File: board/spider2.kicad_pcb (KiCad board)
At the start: 2 copper layers, 137 x 75.5 mm, 121 parts, among them J1 NRJ6HH-1, J10 PJ-320A, J11 PJ358, J12 PJ358, J13 PJ358, J14 PJ358, J15 PJ358, J16 PJ358, J19 PJ358, J2 NRJ6HH-1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

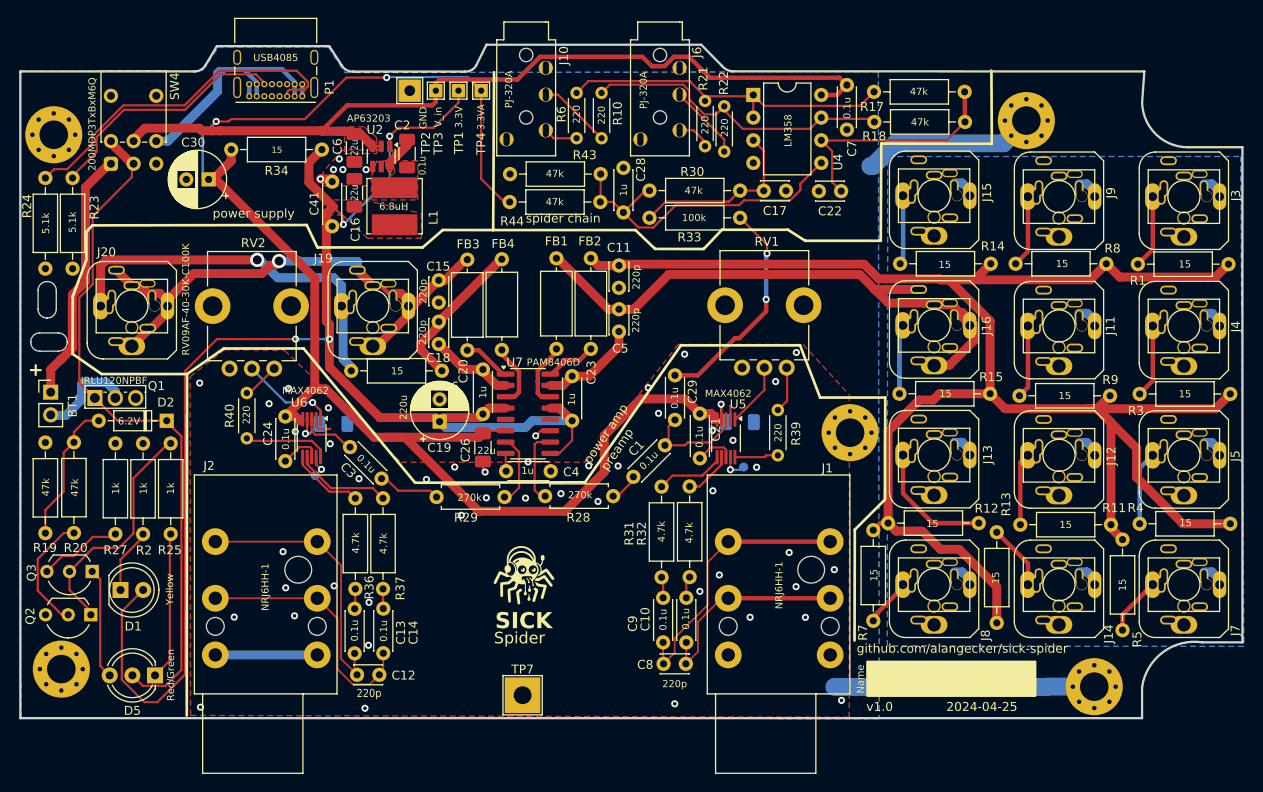
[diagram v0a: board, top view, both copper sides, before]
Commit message: shorter traces + silkscreen updates
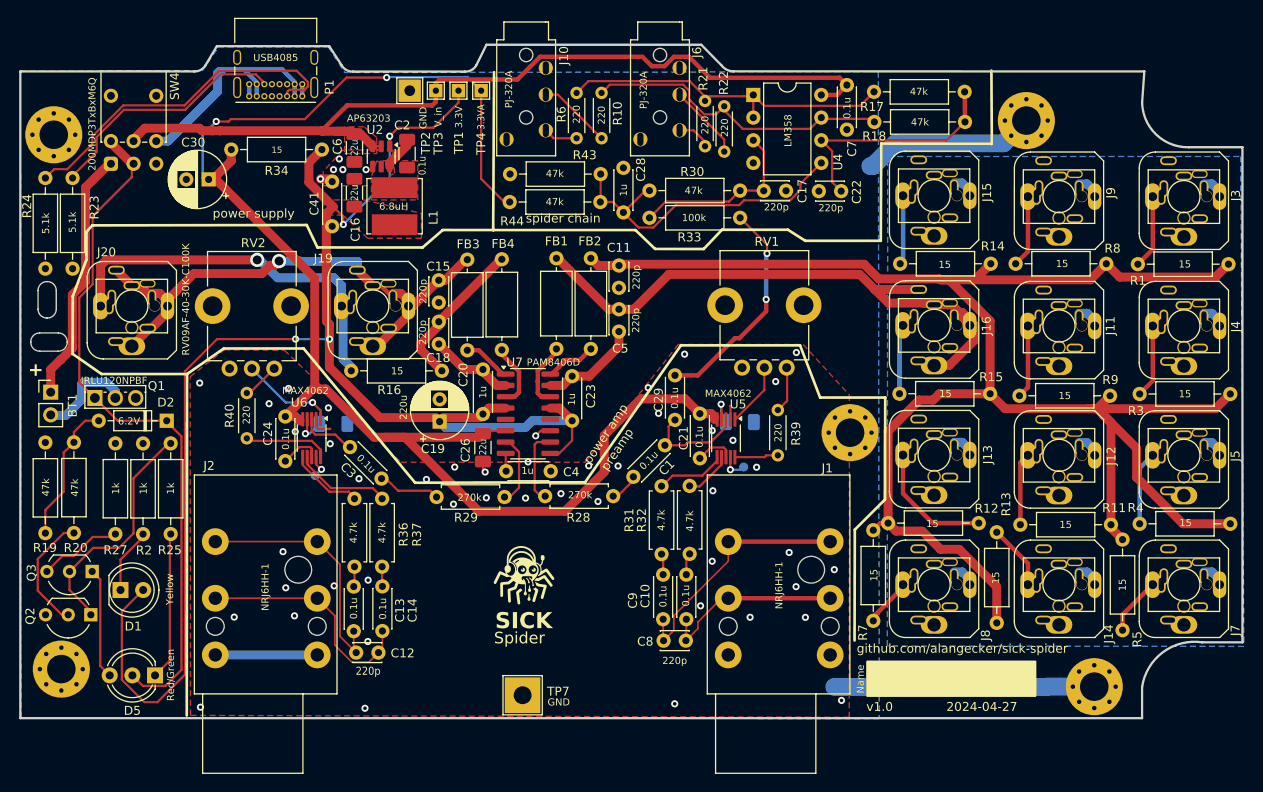
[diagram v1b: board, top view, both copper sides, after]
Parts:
- R31, R32, R36, R37: footprint Resistor_THT:R_Axial_DIN0207_L6.3mm_D2.5mm_P10.16mm_Horizontal -> Resistor_THT:R_Axial_DIN0207_L6.3mm_D2.5mm_P7.62mm_Horizontal
- moved R32 2.60 mm to (212.7, 84.7)
- moved C10 2.60 mm to (212.3, 92.0)
- moved C8 2.60 mm to (209.8, 94.4)
- moved C9 2.60 mm to (209.7, 92.0)
- moved R31 2.60 mm to (209.5, 84.7)
- moved C14 2.49 mm to (178.2, 93.3)
- moved C12 2.49 mm to (175.3, 95.7)
- moved R37 2.49 mm to (178.2, 86.1)
- moved C13 2.49 mm to (175.0, 93.3)
- moved R36 2.49 mm to (175.1, 86.1)
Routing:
- net /Preamp Interpreter/IN+: track 30.6 -> 28.0 mm
- net /Preamp Interpreter/IN-: track 23.6 -> 21.0 mm
- net /Preamp Floor/IN-: track 28.8 -> 26.2 mm
- net /Preamp Floor/IN+: track 30.7 -> 28.2 mm
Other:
- board text added: "2024-04-27"
- board text removed: "2024-04-25"

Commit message: clearer separation of sections, test marks,...
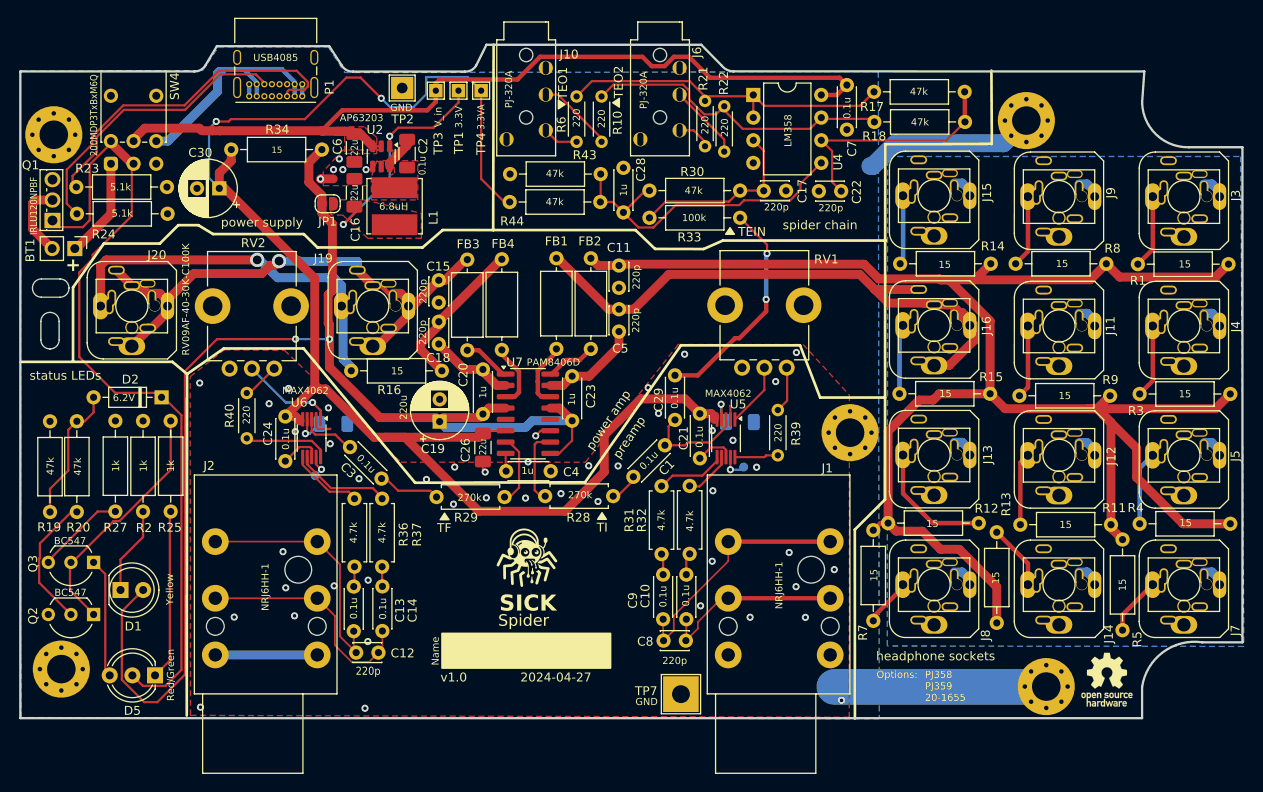
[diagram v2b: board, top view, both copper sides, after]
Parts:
- removed C41: dnp, Capacitor_THT:C_Disc_D4.3mm_W1.9mm_P5.00mm
- added JP1: ~, Jumper:SolderJumper-2_P1.3mm_Open_RoundedPad1.0x1.5mm, F.Cu at (172.1, 45.4)
- added REF**: OSHW-Logo_5.7x6mm_SilkScreen, Symbol:OSHW-Logo_5.7x6mm_SilkScreen, F.Cu at (259.4, 98.8)
- added REF**: OSHW-Logo2_7.3x6mm_SilkScreen, Symbol:OSHW-Logo2_7.3x6mm_SilkScreen, B.Cu at (205.8, 99.2)
- FB2, FB3, FB4: value 3A, >100 Ohm@100MHz -> 3A/≥100 Ohm
- moved Q1 20.5 mm to (141.2, 47.3), turned to 90 degrees
- moved TP7 17.8 mm to (211.7, 100.4)
- moved BT1 16.3 mm to (143.8, 50.5), turned to -90 degrees
- moved R24 15.0 mm to (154.2, 46.5), turned to 180 degrees
- moved R23 14.0 mm to (154.1, 43.5), turned to 180 degrees
- moved H4 5.38 mm to (252.7, 99.5)
- moved D2 2.69 mm to (153.5, 67.1)
- moved R25 2.53 mm to (154.5, 79.9)
- moved R27 2.53 mm to (148.3, 79.9)
- moved R2 2.52 mm to (151.4, 69.8)
- moved R19 2.43 mm to (141.0, 80.0)
- moved R20 2.38 mm to (144.0, 69.8)
- moved C30 1.56 mm to (159.9, 43.7)
- moved Q3 1.03 mm to (145.9, 85.6)
- moved TP2 0.90 mm to (180.4, 32.5)
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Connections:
- C16 pad 2: +3.3V -> Net-(JP1-A)
- L1 pad 2: +3.3V -> Net-(JP1-A)
- TP1 pad 1: +3.3V -> Net-(JP1-A)
- U2 pad 1: +3.3V -> Net-(JP1-A)
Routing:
- net +3.3V: track 171.8 -> 145.1 mm, vias 4 -> 2
- net Net-(JP1-A): track 0.00 -> 26.4 mm, vias 0 -> 2
- net Net-(BT1-+): track 28.3 -> 11.3 mm
- net +BATT: track 77.5 -> 91.8 mm
- net GND: track 101.3 -> 96.0 mm, vias 51 -> 50
- net +3.3VA: track 167.5 -> 170.7 mm
- net Net-(P1-CC): track 39.0 -> 41.6 mm
- net Net-(BT1--): track 11.0 -> 8.39 mm
- net Net-(D5-K1): track 16.6 -> 19.1 mm
- net Net-(D1-K): track 7.31 -> 9.84 mm
- net Net-(Q2-B): track 13.3 -> 15.1 mm
- net Net-(Q2-C): track 26.7 -> 27.9 mm
- net Net-(P1-VCONN): track 27.9 -> 29.1 mm
- net Net-(D5-K2): track 12.5 -> 13.4 mm
- net Net-(D2-A): track 16.0 -> 15.4 mm
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- added copper zone on F.Cu, net Net-(JP1-A)
- removed copper zone on F.Cu, net +3.3V
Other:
- outline, holes or cut-outs redrawn
- board text added: "Options:"
- board text added: "PJ358 PJ359 20-1655"
- board text added: "TEIN"
- board text added: "TEO1"
- board text added: "TEO2"
- board text added: "TF"
- board text added: "TI"
- board text added: "headphone sockets"
- board text added: "status LEDs"

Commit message: some cleanups, cheaper MOSFET,  datasheet links,
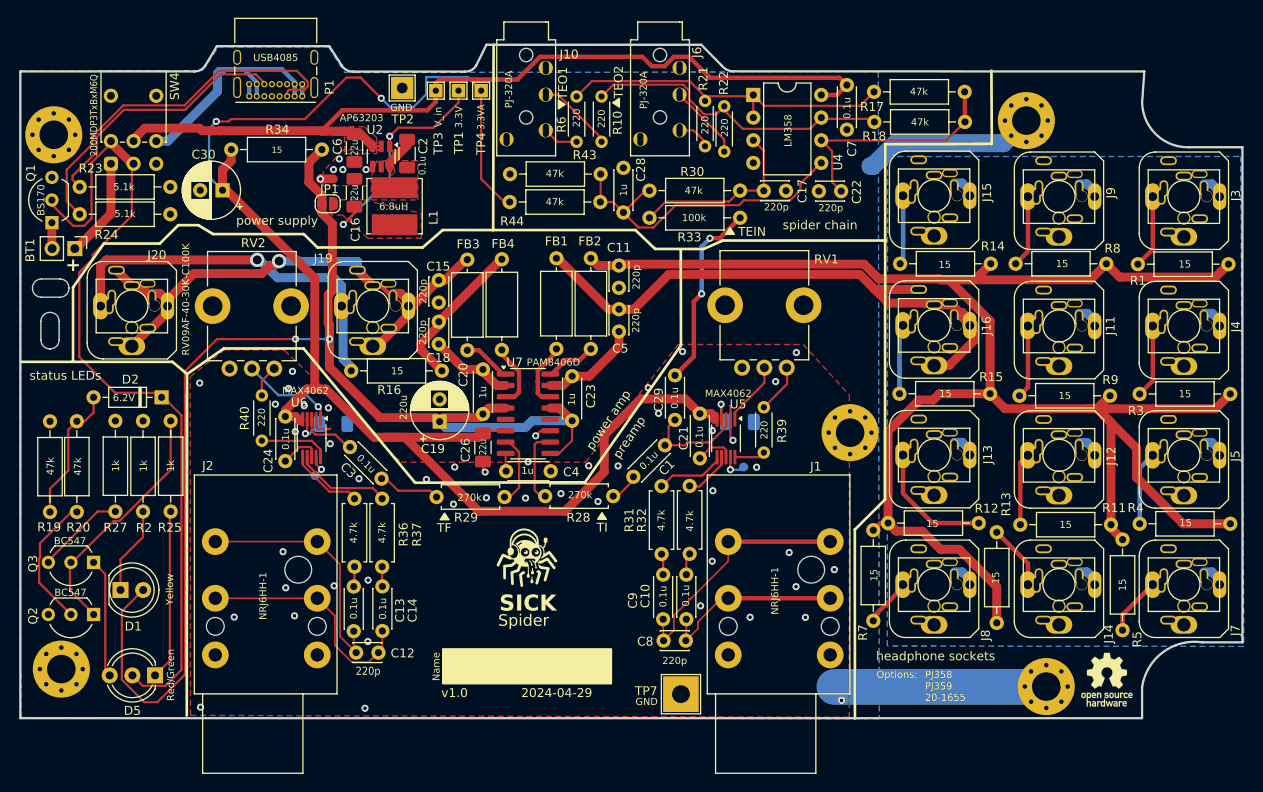
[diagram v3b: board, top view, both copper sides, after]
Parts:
- J1, J2: footprint Connector_Audio:Jack_6.35mm_Neutrik_NRJ6HH_Horizontal -> Connector_Audio:Jack_6.35mm_Neutrik_NRJ6HH-1_Horizontal
- Q1: value IRLU120NPBF -> BS170; footprint Package_TO_SOT_THT:TO-251-3_Vertical -> Package_TO_SOT_THT:TO-92_Inline_Wide
- moved R40 1.71 mm to (164.7, 72.0)
- moved R39 1.60 mm to (221.0, 73.3)
- moved C30 0.42 mm to (160.3, 43.9)
- moved R23 0.38 mm to (154.5, 43.5)
- moved R24 0.31 mm to (154.5, 46.6)
- moved Q1 0.26 mm to (141.2, 47.5)
- renumbered REF** to LOGO1, REF** to LOGO2
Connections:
- Q1 pad 1: +BATT -> Net-(BT1--)
- Q1 pad 2: Net-(BT1--) -> +BATT
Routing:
- net GND: track 96.0 -> 87.0 mm, vias 50 -> 52
- net Net-(BT1--): track 8.39 -> 2.91 mm
- net Net-(C29-Pad1): track 25.0 -> 21.3 mm
- net Net-(U6-G1): track 9.62 -> 7.82 mm
- net Net-(U5-G1): track 4.89 -> 3.45 mm
- net +BATT: track 91.8 -> 93.0 mm
- net Net-(R40-Pad2): track 4.20 -> 3.58 mm
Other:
- board text added: "2024-04-29"
- board text removed: "2024-04-27"

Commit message: 1.0: fixing wrong NRJ6HH-1 symbol
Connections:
- J1 pad G: (no net) -> GND
- J2 pad G: (no net) -> GND
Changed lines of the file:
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@@
 			)
 		)
-		(property "Datasheet" "https://www.neutrik.com/media/9131/download/st-nrj6hh-1.PDF?v=2"
+		(property "Datasheet" "https://www.neutrik.com/en/product/nrj6hh-1"
 			(at 0 0 -90)
 			(unlocked yes)
@@
 			)
 		)
-		(property "Description" "Slim Jacks, 6.35mm (1/4in) stereo jack, switched, half threaded nose"
+		(property "Description" "Slim Jacks, 6.35mm (1/4in) stereo jack, switched, half threaded nose, sleeve contact/front panel connection"
 			(at 0 0 -90)
 			(unlocked yes)
@@
 			(layers "*.Cu" "*.Mask")
 			(remove_unused_layers no)
+			(net 4 "GND")
+			(pintype "passive")
 		)
 		(pad "R" thru_hole circle
@@
 			)
 		)
-		(property "Datasheet" "https://www.neutrik.com/en/product/nrj6hh"
+		(property "Datasheet" "https://www.neutrik.com/en/product/nrj6hh-1"
 			(at 0 0 -90)
 			(unlocked yes)
@@
 			)
 		)
-		(property "Description" "Slim Jacks, 6.35mm (1/4in) stereo jack, switched, half threaded nose"
+		(property "Description" "Slim Jacks, 6.35mm (1/4in) stereo jack, switched, half threaded nose, sleeve contact/front panel connection"
 			(at 0 0 -90)
 			(unlocked yes)
@@
 			(layers "*.Cu" "*.Mask")
 			(remove_unused_layers no)
+			(net 4 "GND")
+			(pintype "passive")
 		)
 		(pad "R" thru_hole circle

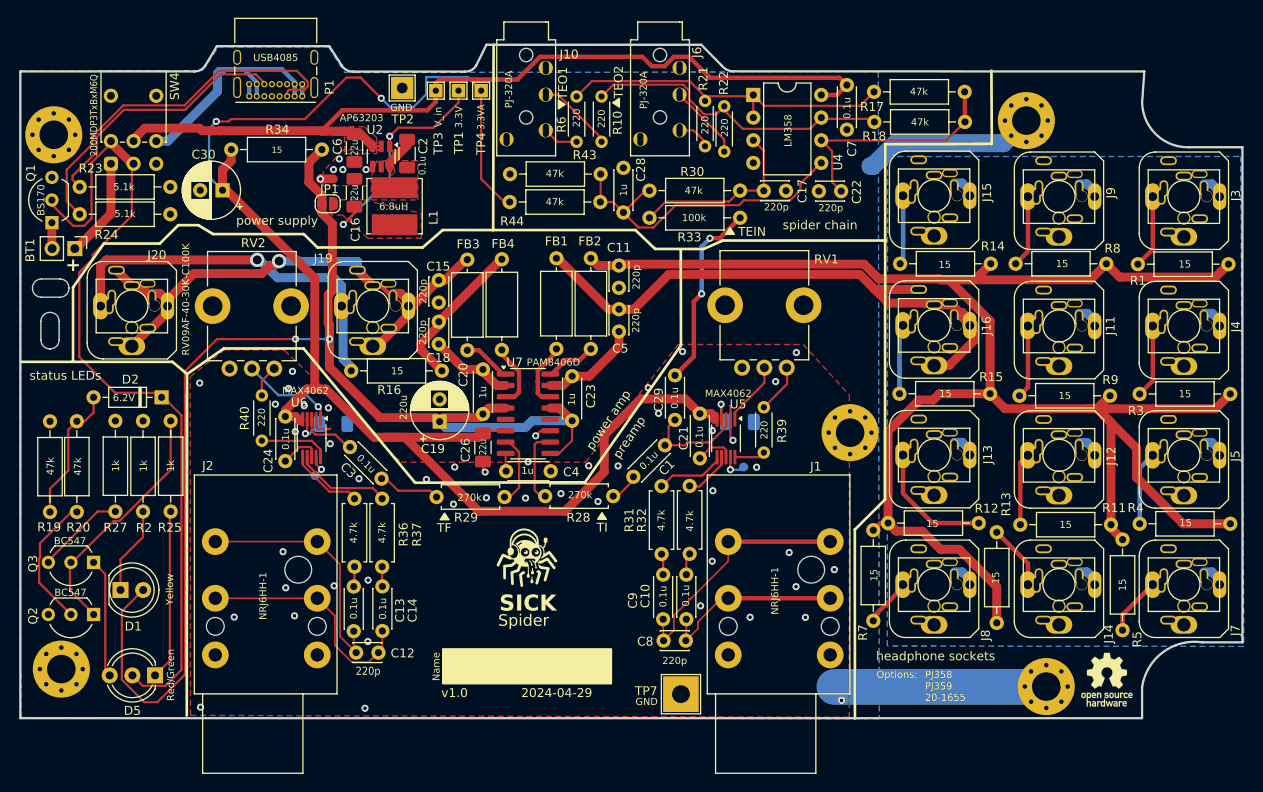
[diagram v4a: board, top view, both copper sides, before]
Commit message: remove PJ359 footprints
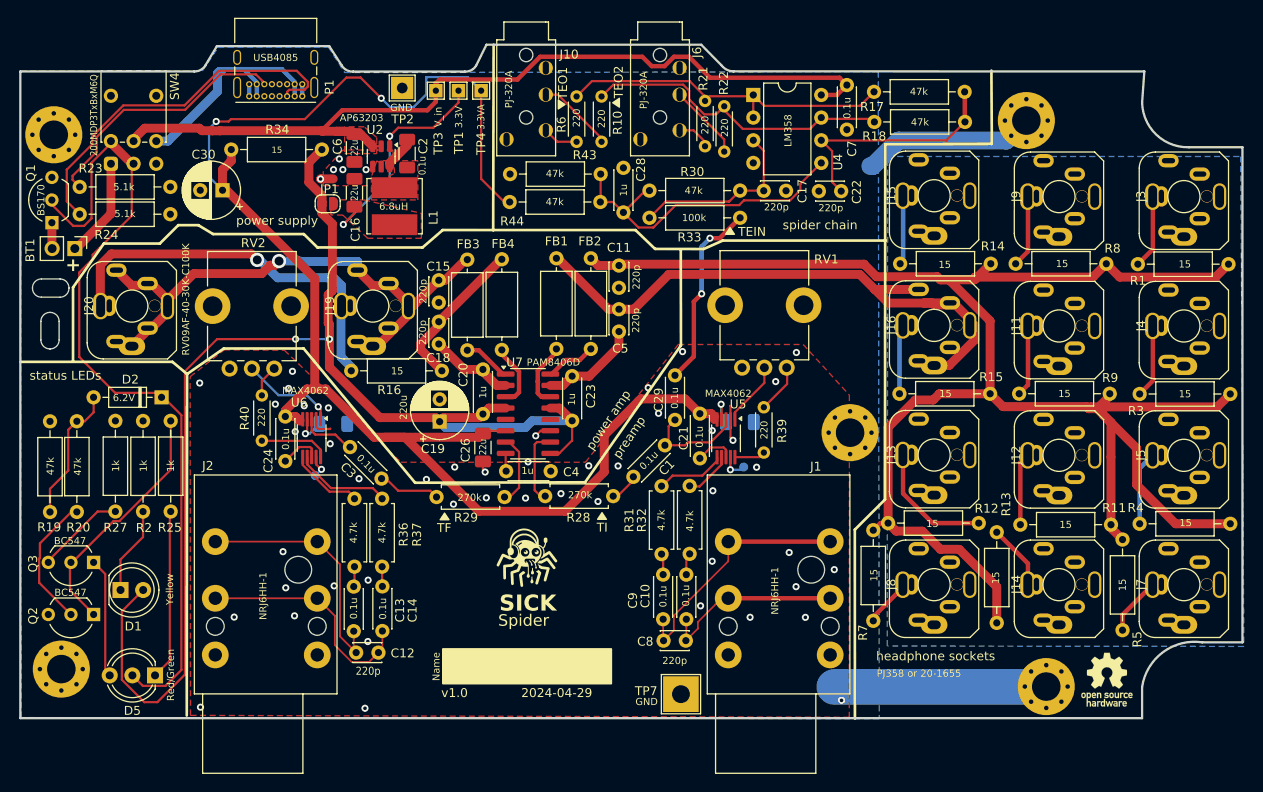
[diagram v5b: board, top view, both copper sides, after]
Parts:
- J11, J12, J13, J14, J15, J16, J19, J20, J3, J4, J5, J7, J8, J9: footprint custom:Jack_3.5mm_Hybrid_PJ358_PJ359_20-1655 -> custom:Jack_3.5mm_Hybrid_PJ358_20-1655
- moved R9 0.23 mm to (249.6, 66.7)
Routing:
- net Net-(C5-Pad2): track 104.3 -> 68.8 mm
- net Net-(C15-Pad2): track 64.4 -> 62.6 mm
- net Net-(C11-Pad1): track 206.1 -> 207.0 mm
- net Net-(J19-PadS): track 43.3 -> 44.1 mm
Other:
- board text added: "PJ358 or 20-1655"
- board text removed: "Options:"
- board text removed: "PJ358 PJ359 20-1655"

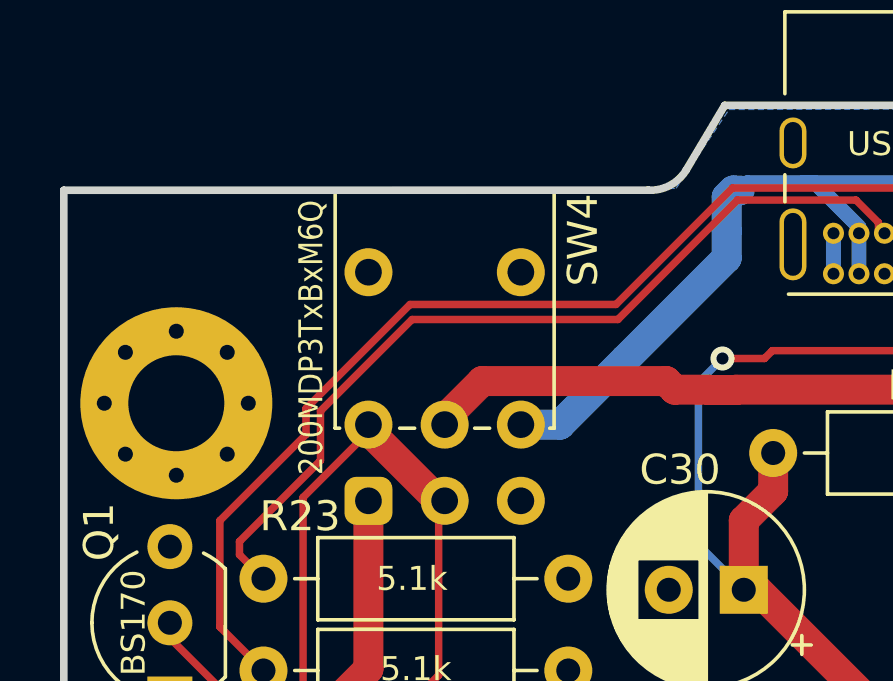
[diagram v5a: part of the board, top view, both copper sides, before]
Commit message: label switch positions (BAT / USB)
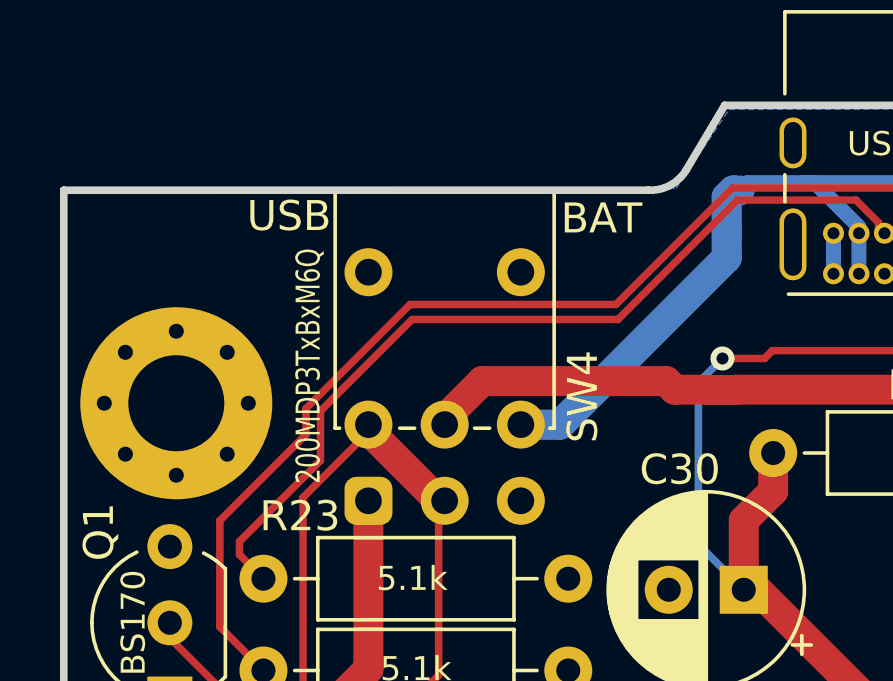
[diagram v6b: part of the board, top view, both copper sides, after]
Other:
- board text added: "BAT"
- board text added: "USB"
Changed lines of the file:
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@@
 		(tags "IP67 ultra-miniture horizontal")
 		(property "Reference" "SW4"
-			(at 8.6934 7.1506 -90)
+			(at 3.4734 7.1506 -90)
 			(layer "F.SilkS")
 			(effects
@@
 		)
 		(property "Value" "200MDP3TxBxM6Q"
-			(at 5.4434 -1.9094 -90)
+			(at 4.4934 -1.9994 270)
 			(layer "F.SilkS")
 			(effects
 				(font
-					(size 0.8 0.7)
+					(size 0.8 0.6)
 					(thickness 0.1)
 				)
@@
 		)
 	)
+	(gr_text "BAT"
+		(at 154.21 32.12 0)
+		(layer "F.SilkS")
+		(effects
+			(font
+				(size 1 1)
+				(thickness 0.15)
+			)
+			(justify left bottom)
+		)
+	)
 	(gr_text "v1.0"
 		(at 184.821151 100.845524 0)
@@
 		)
 	)
+	(gr_text "USB"
+		(at 146.56 32.04 0)
+		(layer "F.SilkS")
+		(effects
+			(font
+				(size 1 1)
+				(thickness 0.15)
+			)
+			(justify right bottom)
+		)
+	)
